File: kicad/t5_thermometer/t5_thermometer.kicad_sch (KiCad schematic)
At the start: 11 parts, among them J1 Conn_ARM_JTAG_SWD_10, J2 NTCs, J4 Screw_Terminal_01x06, U1 STM32F042F6Px, U2 TSR_1-2433

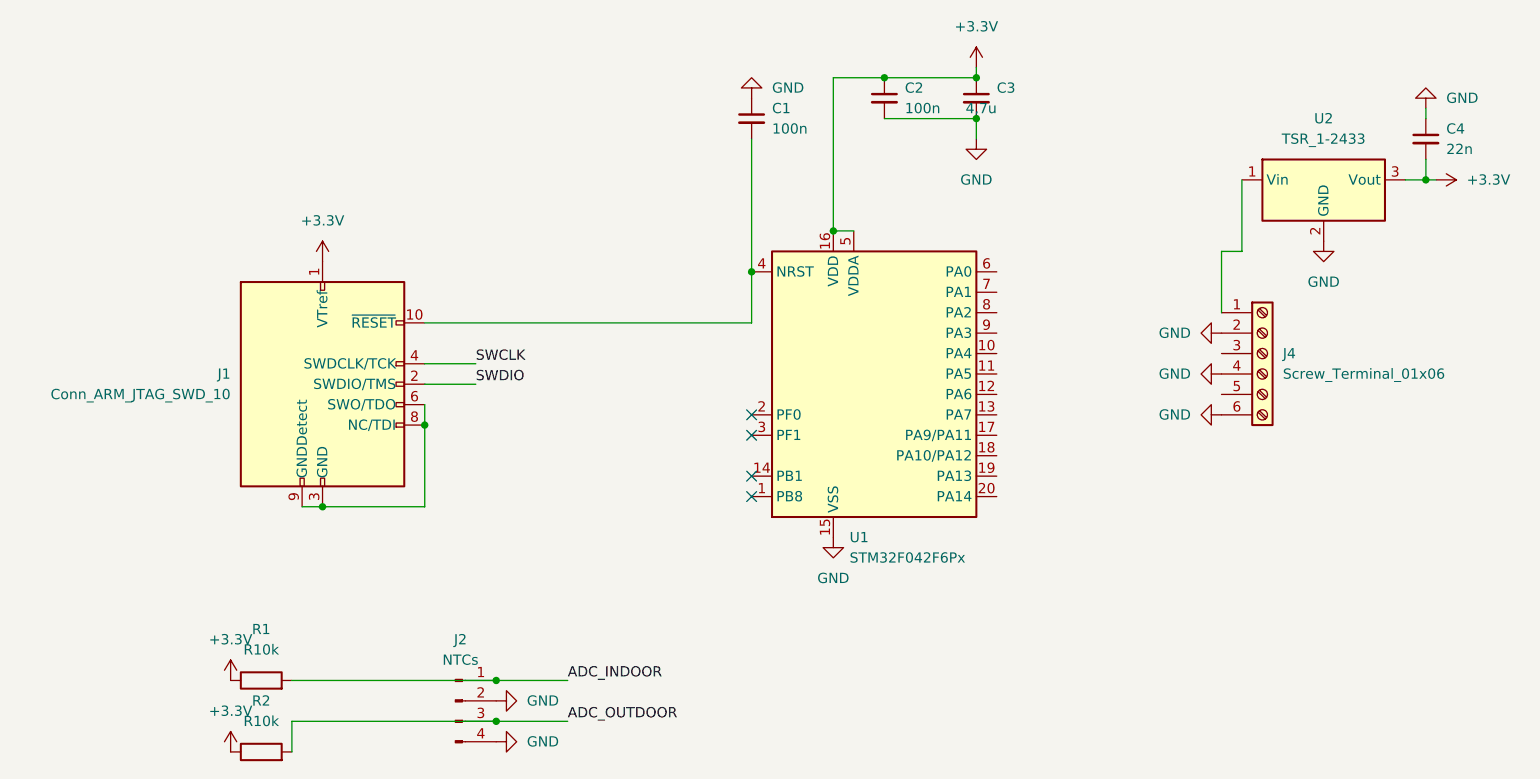
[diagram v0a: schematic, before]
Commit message: Configure all necessary Pins, I2C DMA is missing
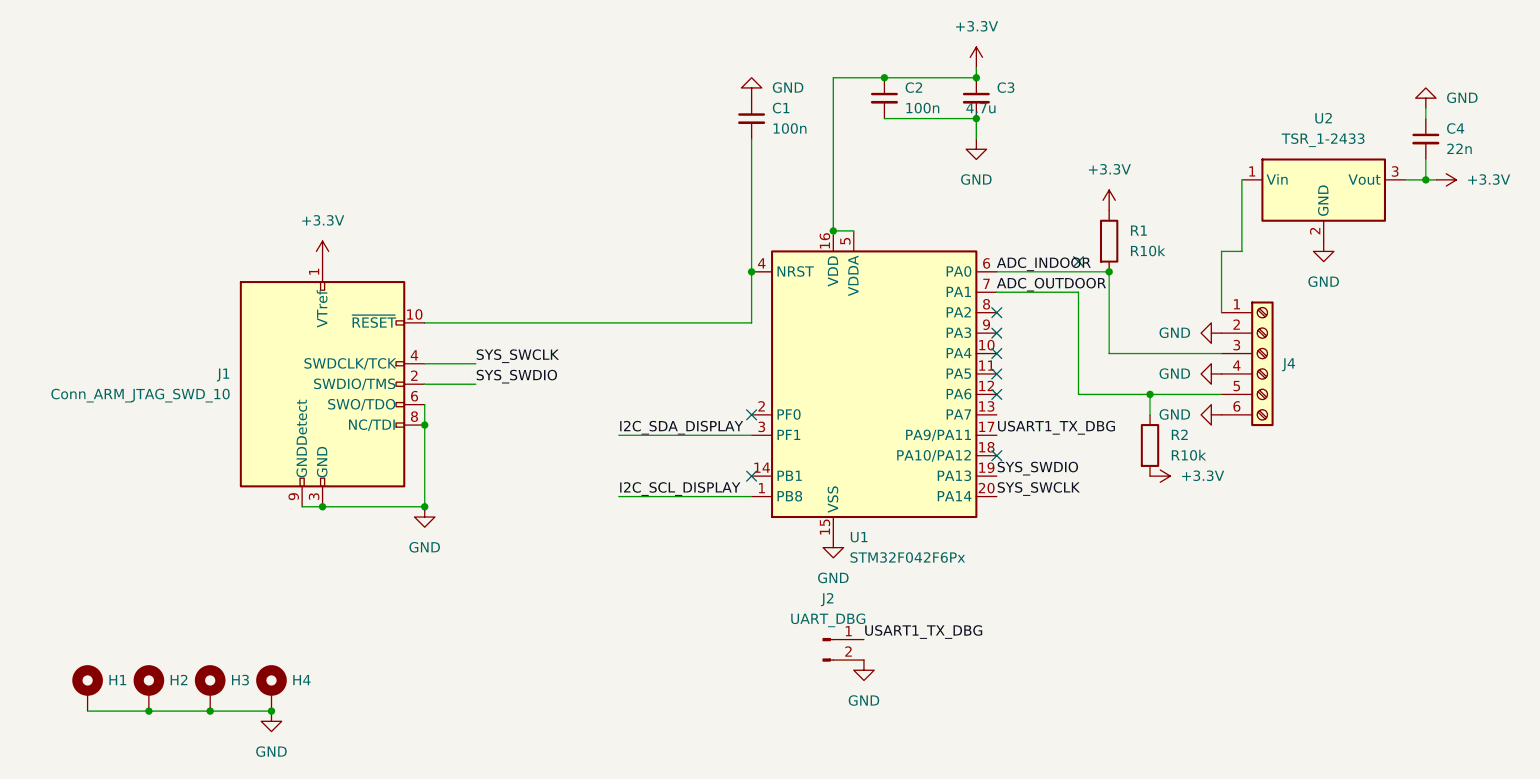
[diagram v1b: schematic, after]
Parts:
- removed J2: NTCs, Connector_PinHeader_2.54mm:PinHeader_1x04_P2.54mm_Vertical, symbol Connector:Conn_01x04_Pin
- added H1, H2, H3, H4: MountingHole_Pad, MountingHole:MountingHole_3.2mm_M3, symbol Mechanical:MountingHole_Pad
- added J2: UART_DBG, Connector_PinHeader_2.54mm:PinHeader_1x02_P2.54mm_Horizontal, symbol Connector:Conn_01x02_Pin
- J4: footprint (none) -> TerminalBlock_Phoenix:TerminalBlock_Phoenix_MKDS-1,5-6-5.08_1x06_P5.08mm_Horizontal
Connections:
- net SWCLK is gone; now on net SYS_SWCLK: J1.4 (SWDCLK/TCK)
- net SWDIO is gone; now on net SYS_SWDIO: J1.2 (SWDIO/TMS)
- net +3.3V: now also R2.2; no longer R2.1
- net ADC_INDOOR: now also J4.3 (Pin_3), U1.6 (PA0)
- net ADC_OUTDOOR: now also J4.5 (Pin_5), R2.1, U1.7 (PA1); no longer R2.2
- net GND: now also J1.3 (GND), J1.5 (GND), J1.6 (SWO/TDO), J1.8 (NC/TDI), J1.9 (GNDDetect), H1.1, H2.1, H3.1, H4.1, J2.2 (Pin_2)
- net I2C_SCL_DISPLAY: now reaches U1.1 (PB8)
- net USART1_TX_DBG: now reaches U1.17 (PA9/PA11)
- net USART1_TX_DBG: now also J2.1 (Pin_1)
- net SYS_SWDIO: now reaches U1.19 (PA13)
- net SYS_SWCLK: now reaches U1.20 (PA14)
- net I2C_SDA_DISPLAY: now reaches U1.3 (PF1)
- no-connect marks 4 -> 9

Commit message: Add configuration and PCB design which was ordered.
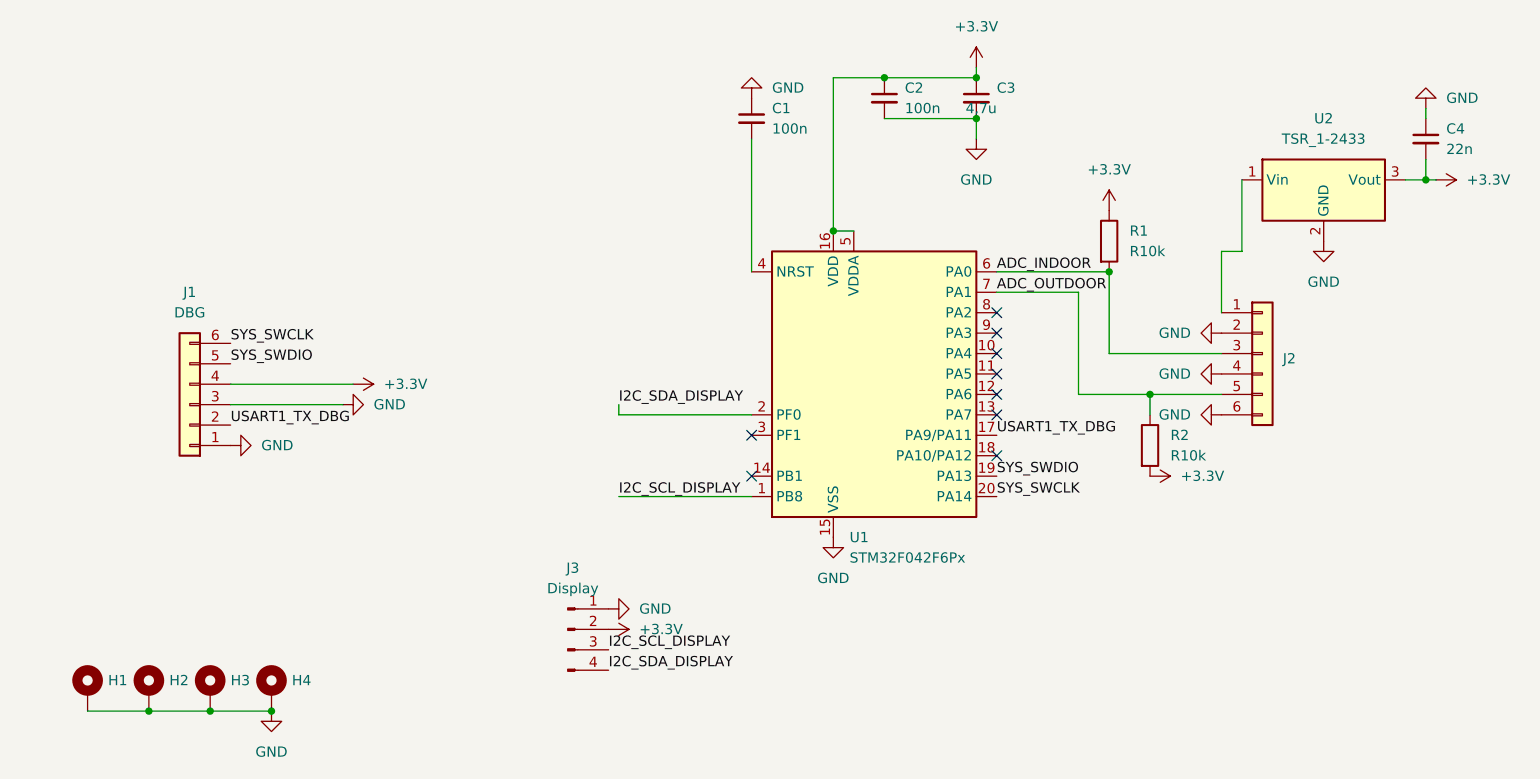
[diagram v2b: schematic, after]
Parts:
- removed J1: Conn_ARM_JTAG_SWD_10, Connector_PinHeader_2.54mm:PinHeader_2x05_P2.54mm_Vertical, symbol Connector:Conn_ARM_JTAG_SWD_10
- removed J2: UART_DBG, Connector_PinHeader_2.54mm:PinHeader_1x02_P2.54mm_Horizontal, symbol Connector:Conn_01x02_Pin
- removed J4: Screw_Terminal_01x06, TerminalBlock_Phoenix:TerminalBlock_Phoenix_MKDS-1,5-6-5.08_1x06_P5.08mm_Horizontal, symbol Connector:Screw_Terminal_01x06
- added J1: DBG, Connector_PinHeader_2.54mm:PinHeader_1x06_P2.54mm_Vertical, symbol Connector_Generic:Conn_01x06
- added J2: ~, Connector_PinHeader_2.54mm:PinHeader_1x06_P2.54mm_Vertical, symbol Connector_Generic:Conn_01x06
- added J3: Display, Connector_PinHeader_2.54mm:PinHeader_1x04_P2.54mm_Vertical, symbol Connector:Conn_01x04_Pin
- H1, H2, H3, H4: footprint MountingHole:MountingHole_3.2mm_M3 -> MountingHole:MountingHole_2.2mm_M2
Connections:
- net +3.3V: now also J1.4 (Pin_4), J3.2 (Pin_2)
- net ADC_INDOOR: now also J2.3 (Pin_3)
- net ADC_OUTDOOR: now also J2.5 (Pin_5)
- net GND: now also J1.1 (Pin_1), J1.3 (Pin_3), J2.2 (Pin_2), J2.4 (Pin_4), J2.6 (Pin_6), J3.1 (Pin_1)
- net I2C_SCL_DISPLAY: now also J3.3 (Pin_3)
- net I2C_SDA_DISPLAY: now also U1.2 (PF0), J3.4 (Pin_4); no longer U1.3 (PF1)
- net SYS_SWCLK: now also J1.6 (Pin_6)
- net SYS_SWDIO: now also J1.5 (Pin_5)
- net USART1_TX_DBG: now also J1.2 (Pin_2)
- net at U2.1 (Vin): now also J2.1 (Pin_1)

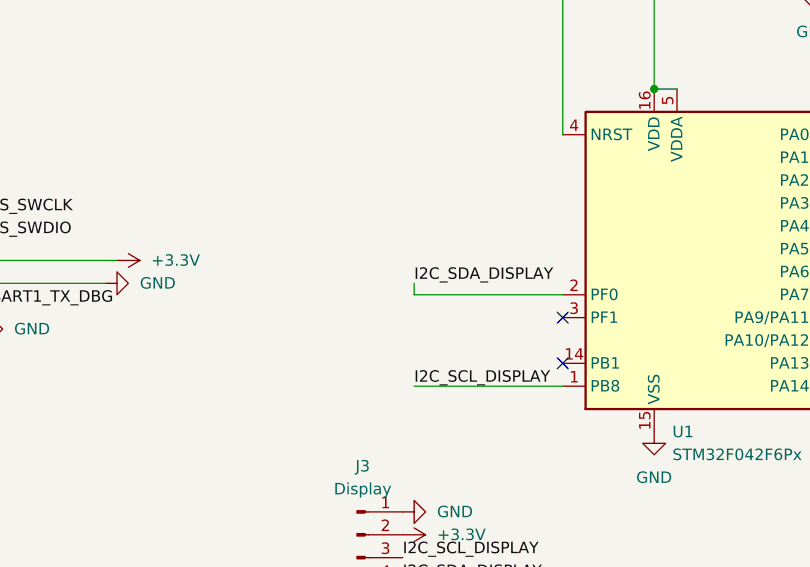
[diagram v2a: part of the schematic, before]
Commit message: schematic change: - Add 4,7k pull up for I2C - Connect PB8 to GND. PB8 was initially planned as I2C SCL, but due to   the fact that it also operates as BOOT0 pin, it cannot be pulled up.
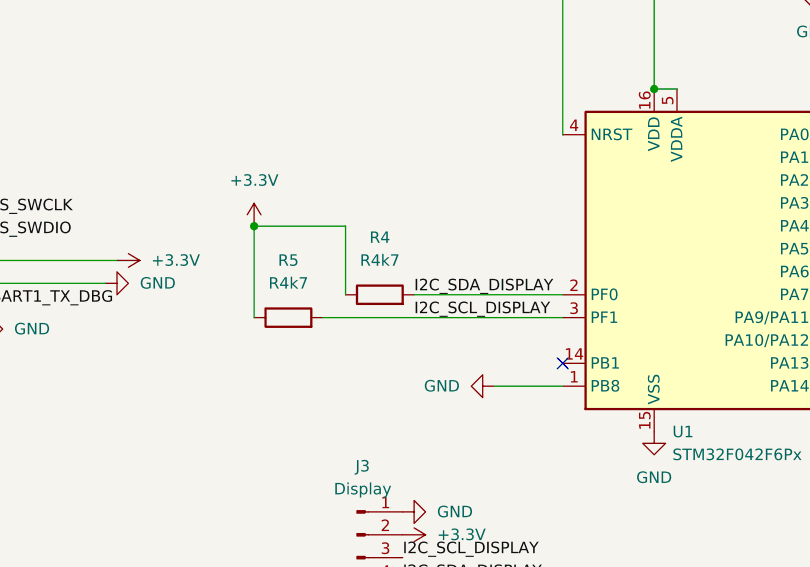
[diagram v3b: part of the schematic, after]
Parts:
- added R4, R5: R4k7, Resistor_SMD:R_0603_1608Metric_Pad0.98x0.95mm_HandSolder, symbol Device:R
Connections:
- net +3.3V: now also R4.1, R5.1
- net GND: now also U1.1 (PB8)
- net I2C_SCL_DISPLAY: now also U1.3 (PF1), R5.2; no longer U1.1 (PB8)
- net I2C_SDA_DISPLAY: now also R4.2
- no-connect marks 9 -> 8

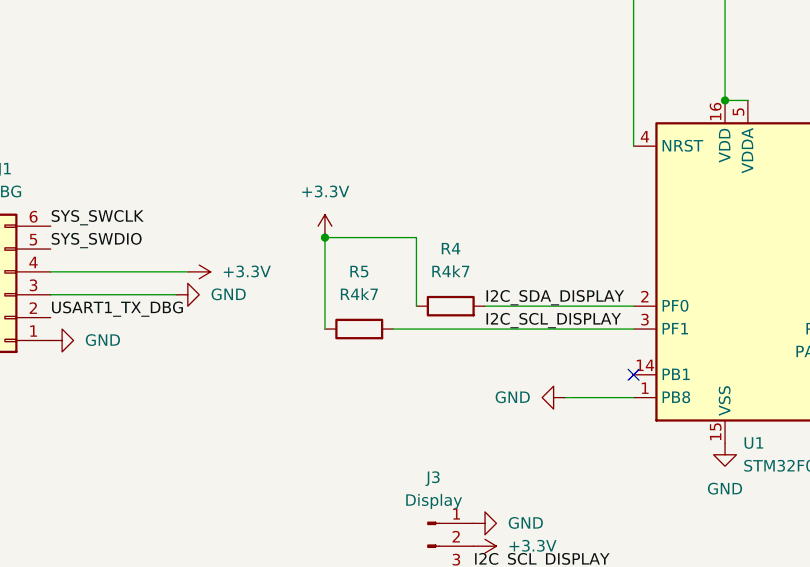
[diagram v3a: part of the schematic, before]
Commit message: free PB8 pin, fix several issues, add configurability to ssd1306 lib
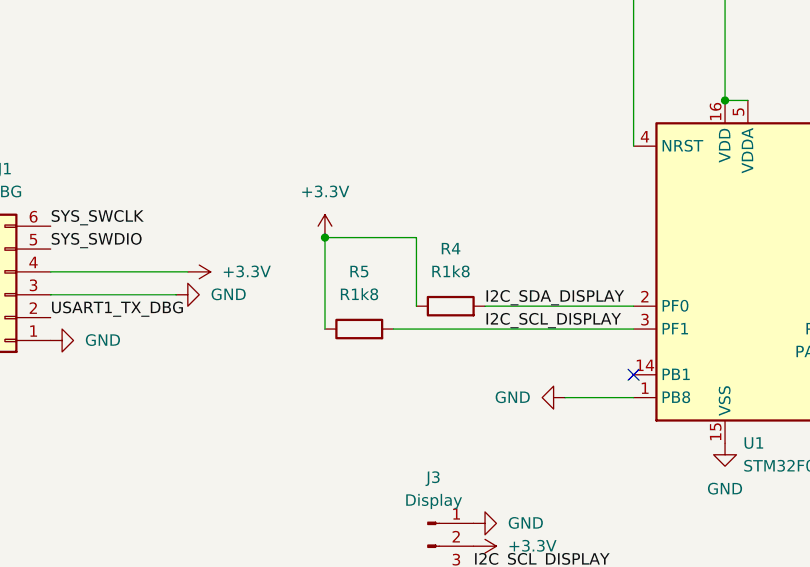
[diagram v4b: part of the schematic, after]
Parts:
- R4, R5: value R4k7 -> R1k8
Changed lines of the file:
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@@
 			)
 		)
-		(property "Value" "R4k7"
+		(property "Value" "R1k8"
 			(at 137.16 95.25 90)
 			(effects
@@
 			)
 		)
-		(property "Value" "R4k7"
+		(property "Value" "R1k8"
 			(at 147.32 92.71 90)
 			(effects
